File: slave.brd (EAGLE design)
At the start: 160 x 100 mm, 12 parts

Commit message: increase size of routes
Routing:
- net A1: track 48.1 -> 43.0 mm
- net D3: track 13.6 -> 17.2 mm
- net A2: track 38.3 -> 36.4 mm
- net RX4: track 20.5 -> 19.1 mm
- net A0: track 48.8 -> 50.1 mm
- net TX0: track 22.4 -> 23.5 mm
- net TX4: track 18.3 -> 17.4 mm
- net A5: track 24.3 -> 25.2 mm
- net D2: track 21.8 -> 22.7 mm
- net RX1: track 20.9 -> 21.5 mm
- net GND: vias 16 -> 14

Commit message: Fix arduino uno pcb not fit
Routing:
- net D1: track 26.7 -> 29.4 mm
- net TX5: track 41.7 -> 39.0 mm
- net D0: track 50.1 -> 52.8 mm
- net D4: track 13.9 -> 12.0 mm
- net D5: track 20.2 -> 18.5 mm
- net D2: track 22.7 -> 23.9 mm
- net TX1: track 20.6 -> 19.4 mm
- net TX0: track 23.5 -> 22.3 mm
- net TX2: track 20.5 -> 19.3 mm
- net GND: track 94.6 -> 95.6 mm
- net TX3: track 18.7 -> 17.8 mm
- net D3: track 17.2 -> 16.6 mm
- added copper zone on layer 16, net N$1
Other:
- board size 160 x 100 mm -> 150 x 100 mm

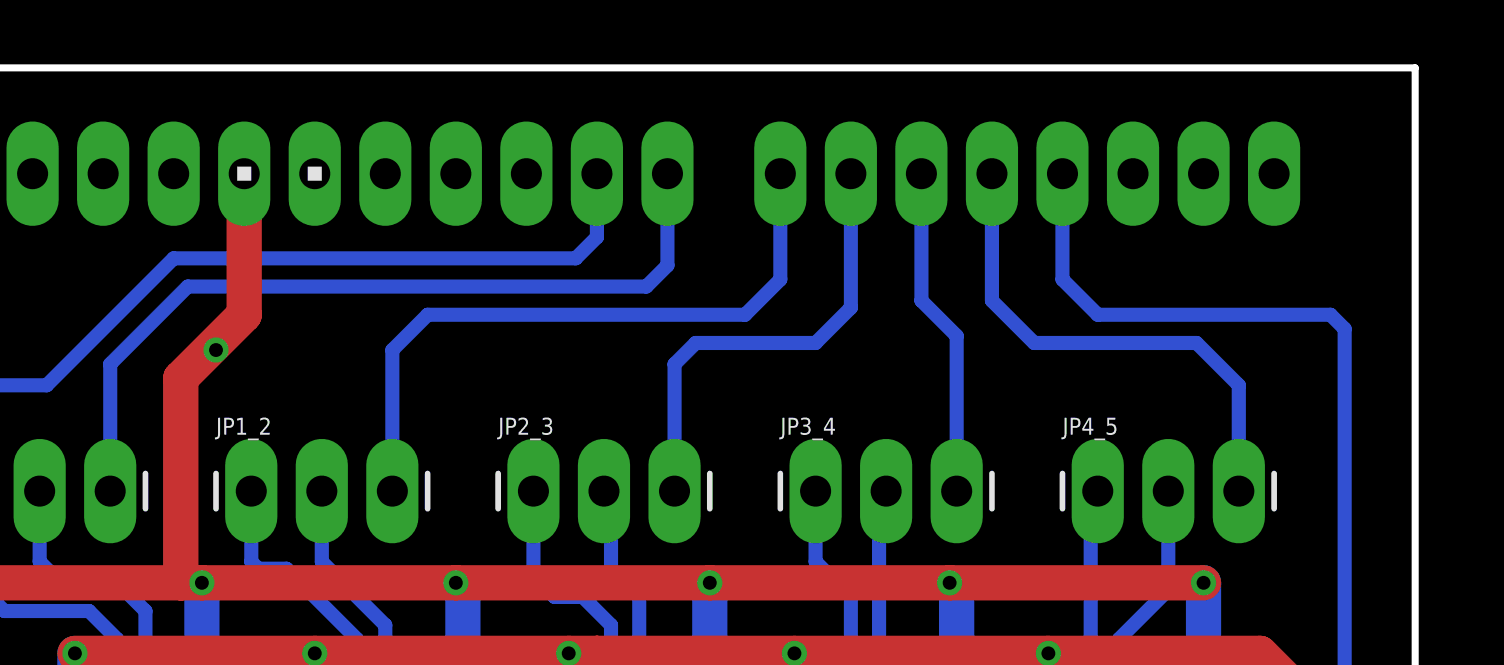
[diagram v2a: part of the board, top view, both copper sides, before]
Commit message: update for CAN Bus shield
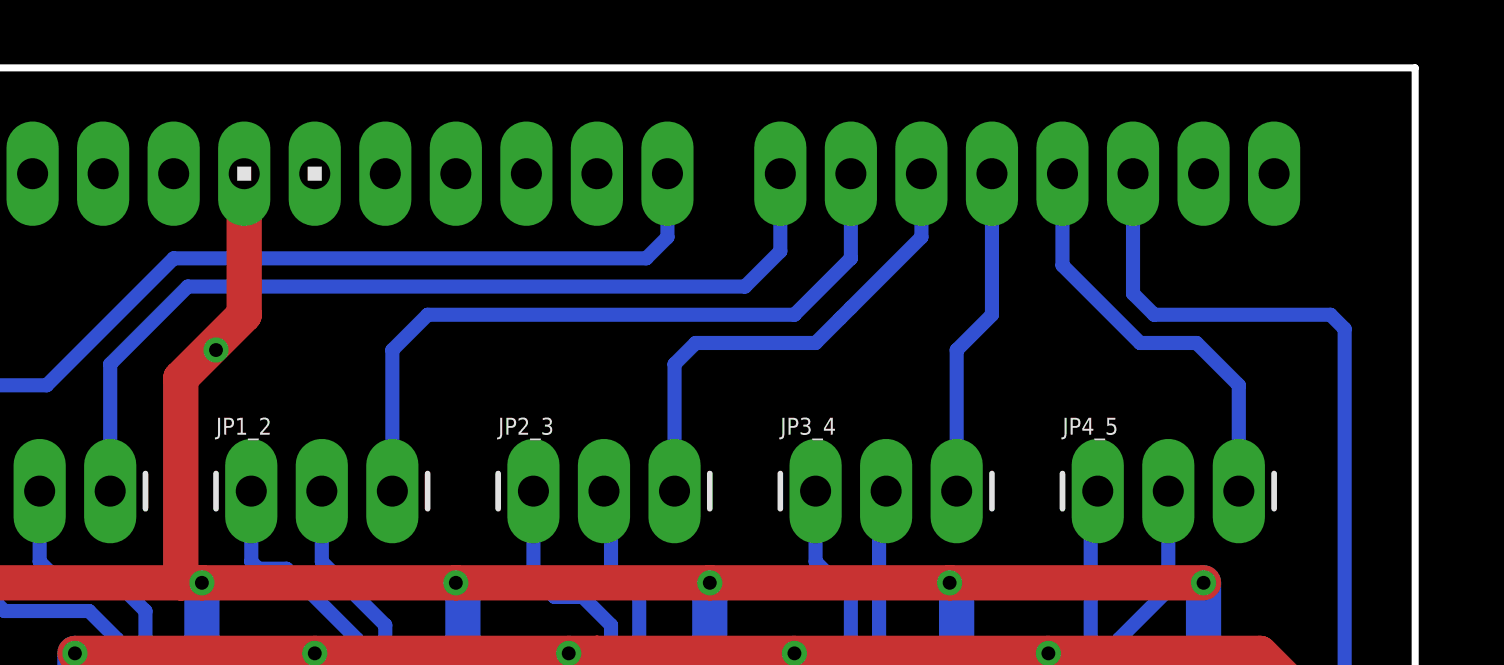
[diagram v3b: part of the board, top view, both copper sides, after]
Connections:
- net D0: now also U$1.22; no longer U$1.23
- net D1: now also U$1.21; no longer U$1.22
- net D2: now also U$1.20; no longer U$1.21
- net D3: now also U$1.19; no longer U$1.20
- net D4: now also U$1.18; no longer U$1.19
- net D5: now also U$1.17; no longer U$1.18
- net TX5: now also U$1.16; no longer U$1.17
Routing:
- net D1: track 29.4 -> 33.2 mm
- net D5: track 18.5 -> 15.3 mm
- net D0: track 52.8 -> 55.4 mm
- net TX5: track 39.0 -> 36.8 mm
- net D2: track 23.9 -> 26.0 mm
- net D3: track 16.6 -> 17.6 mm
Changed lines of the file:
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@@
 <signal name="D5">
 <contactref element="JP4_5" pad="3"/>
-<contactref element="U$1" pad="18"/>
 <wire x1="69.85" y1="59.69" x2="69.85" y2="63.5" width="0.508" layer="16"/>
 <wire x1="69.85" y1="63.5" x2="68.326" y2="65.024" width="0.508" layer="16"/>
-<wire x1="62.484" y1="65.024" x2="68.326" y2="65.024" width="0.508" layer="16"/>
-<wire x1="60.96" y1="71.12" x2="60.96" y2="66.548" width="0.508" layer="16"/>
-<wire x1="60.96" y1="66.548" x2="62.484" y2="65.024" width="0.508" layer="16"/>
+<wire x1="66.294" y1="65.024" x2="68.326" y2="65.024" width="0.508" layer="16"/>
+<contactref element="U$1" pad="17"/>
+<wire x1="63.5" y1="71.12" x2="63.5" y2="67.818" width="0.508" layer="16"/>
+<wire x1="63.5" y1="67.818" x2="66.294" y2="65.024" width="0.508" layer="16"/>
 </signal>
 <signal name="D4">
 <contactref element="JP3_4" pad="3"/>
-<contactref element="U$1" pad="19"/>
-<wire x1="59.69" y1="65.278" x2="59.69" y2="59.69" width="0.508" layer="16"/>
-<wire x1="58.42" y1="71.12" x2="58.42" y2="66.548" width="0.508" layer="16"/>
-<wire x1="58.42" y1="66.548" x2="59.69" y2="65.278" width="0.508" layer="16"/>
+<wire x1="59.69" y1="64.77" x2="59.69" y2="59.69" width="0.508" layer="16"/>
+<contactref element="U$1" pad="18"/>
+<wire x1="60.96" y1="71.12" x2="60.96" y2="66.04" width="0.508" layer="16"/>
+<wire x1="60.96" y1="66.04" x2="59.69" y2="64.77" width="0.508" layer="16"/>
 </signal>
 <signal name="D3">
 <contactref element="JP2_3" pad="3"/>
-<contactref element="U$1" pad="20"/>
 <wire x1="49.53" y1="59.69" x2="49.53" y2="64.262" width="0.508" layer="16"/>
 <wire x1="50.292" y1="65.024" x2="49.53" y2="64.262" width="0.508" layer="16"/>
-<wire x1="55.88" y1="71.12" x2="55.88" y2="66.294" width="0.508" layer="16"/>
-<wire x1="55.88" y1="66.294" x2="54.61" y2="65.024" width="0.508" layer="16"/>
+<wire x1="55.88" y1="66.294" x2="55.499" y2="65.913" width="0.508" layer="16"/>
+<wire x1="55.499" y1="65.913" x2="54.61" y2="65.024" width="0.508" layer="16"/>
 <wire x1="54.61" y1="65.024" x2="50.292" y2="65.024" width="0.508" layer="16"/>
+<contactref element="U$1" pad="19"/>
+<wire x1="58.42" y1="71.12" x2="58.42" y2="68.834" width="0.508" layer="16"/>
+<wire x1="58.42" y1="68.834" x2="55.88" y2="66.294" width="0.508" layer="16"/>
 </signal>
 <signal name="D2">
 <contactref element="JP1_2" pad="3"/>
-<contactref element="U$1" pad="21"/>
 <wire x1="39.37" y1="59.69" x2="39.37" y2="64.77" width="0.508" layer="16"/>
 <wire x1="39.37" y1="64.77" x2="40.64" y2="66.04" width="0.508" layer="16"/>
-<wire x1="40.64" y1="66.04" x2="52.07" y2="66.04" width="0.508" layer="16"/>
-<wire x1="53.34" y1="71.12" x2="53.34" y2="67.31" width="0.508" layer="16"/>
-<wire x1="53.34" y1="67.31" x2="52.07" y2="66.04" width="0.508" layer="16"/>
+<wire x1="40.64" y1="66.04" x2="53.848" y2="66.04" width="0.508" layer="16"/>
+<contactref element="U$1" pad="20"/>
+<wire x1="55.88" y1="71.12" x2="55.88" y2="68.072" width="0.508" layer="16"/>
+<wire x1="55.88" y1="68.072" x2="53.848" y2="66.04" width="0.508" layer="16"/>
 </signal>
 <signal name="D1">
 <contactref element="JP0_1" pad="3"/>
-<contactref element="U$1" pad="22"/>
 <wire x1="29.21" y1="59.69" x2="29.21" y2="64.262" width="0.508" layer="16"/>
 <wire x1="32.004" y1="67.056" x2="29.21" y2="64.262" width="0.508" layer="16"/>
-<wire x1="49.276" y1="71.12" x2="49.276" y2="67.818" width="0.508" layer="16"/>
-<wire x1="49.276" y1="67.818" x2="48.514" y2="67.056" width="0.508" layer="16"/>
-<wire x1="48.514" y1="67.056" x2="32.004" y2="67.056" width="0.508" layer="16"/>
+<wire x1="52.07" y1="67.056" x2="32.004" y2="67.056" width="0.508" layer="16"/>
+<contactref element="U$1" pad="21"/>
+<wire x1="53.34" y1="71.12" x2="53.34" y2="68.326" width="0.508" layer="16"/>
+<wire x1="53.34" y1="68.326" x2="52.07" y2="67.056" width="0.508" layer="16"/>
 </signal>
 <signal name="D0">
 <contactref element="J0" pad="4"/>
-<contactref element="U$1" pad="23"/>
 <wire x1="24.13" y1="43.18" x2="21.844" y2="43.18" width="0.508" layer="16"/>
 <wire x1="21.844" y1="43.18" x2="20.828" y2="44.196" width="0.508" layer="16"/>
@@
 <wire x1="21.844" y1="63.5" x2="26.924" y2="63.5" width="0.508" layer="16"/>
 <wire x1="31.496" y1="68.072" x2="26.924" y2="63.5" width="0.508" layer="16"/>
-<wire x1="46.736" y1="71.12" x2="46.736" y2="68.834" width="0.508" layer="16"/>
-<wire x1="46.736" y1="68.834" x2="45.974" y2="68.072" width="0.508" layer="16"/>
-<wire x1="45.974" y1="68.072" x2="31.496" y2="68.072" width="0.508" layer="16"/>
+<wire x1="48.514" y1="68.072" x2="31.496" y2="68.072" width="0.508" layer="16"/>
+<contactref element="U$1" pad="22"/>
+<wire x1="49.276" y1="71.12" x2="49.276" y2="68.834" width="0.508" layer="16"/>
+<wire x1="49.276" y1="68.834" x2="48.514" y2="68.072" width="0.508" layer="16"/>
 </signal>
 <signal name="TX0">
@@
 <signal name="TX5">
 <contactref element="J5" pad="5"/>
-<contactref element="U$1" pad="17"/>
 <wire x1="68.58" y1="45.72" x2="72.644" y2="45.72" width="0.508" layer="16"/>
 <wire x1="72.644" y1="45.72" x2="73.66" y2="46.736" width="0.508" layer="16"/>
 <wire x1="73.66" y1="46.736" x2="73.66" y2="65.532" width="0.508" layer="16"/>
 <wire x1="73.66" y1="65.532" x2="73.152" y2="66.04" width="0.508" layer="16"/>
-<wire x1="64.77" y1="66.04" x2="73.152" y2="66.04" width="0.508" layer="16"/>
-<wire x1="63.5" y1="71.12" x2="63.5" y2="67.31" width="0.508" layer="16"/>
-<wire x1="63.5" y1="67.31" x2="64.77" y2="66.04" width="0.508" layer="16"/>
+<wire x1="66.802" y1="66.04" x2="73.152" y2="66.04" width="0.508" layer="16"/>
+<contactref element="U$1" pad="16"/>
+<wire x1="66.04" y1="71.12" x2="66.04" y2="66.802" width="0.508" layer="16"/>
+<wire x1="66.04" y1="66.802" x2="66.802" y2="66.04" width="0.508" layer="16"/>
 </signal>
 <signal name="GND_1">
